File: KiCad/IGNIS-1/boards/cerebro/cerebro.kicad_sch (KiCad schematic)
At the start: 14 parts, among them J40 Backplane_2x10, J50 J_PWR_2x4, Q1 MMBT3904, U10 ESP32-WROOM-32E DevKit 40p

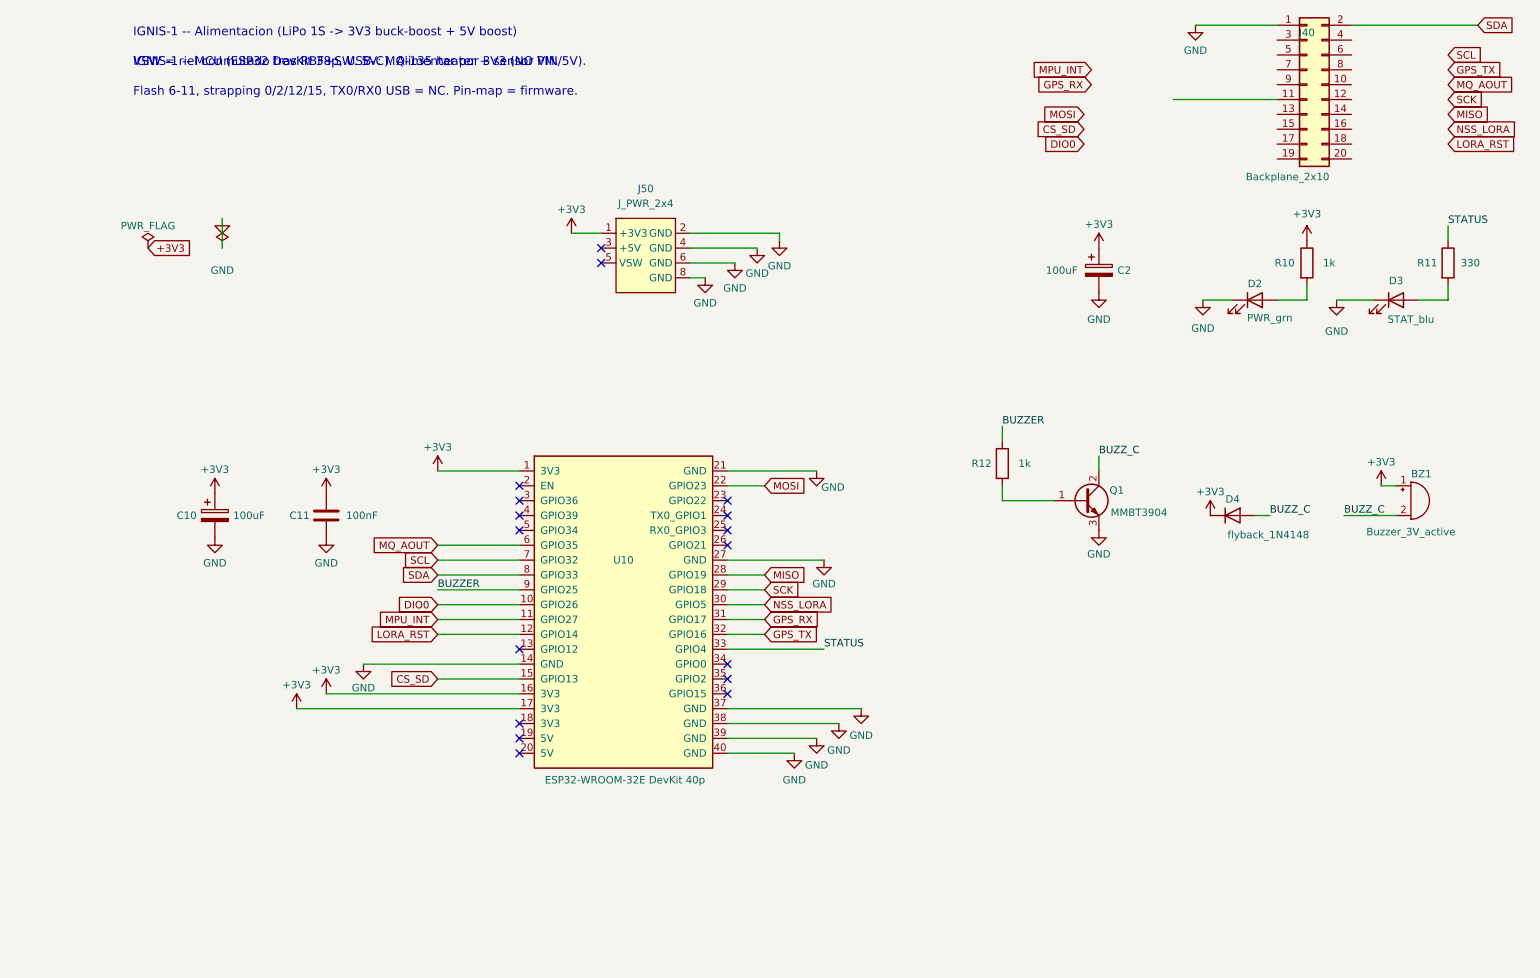
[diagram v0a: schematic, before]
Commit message: wip: recableo backplane split en progreso (GUI) + doc con move TPS63020
Co-Authored-By: Claude Opus 4.8 <noreply@anthropic.com>
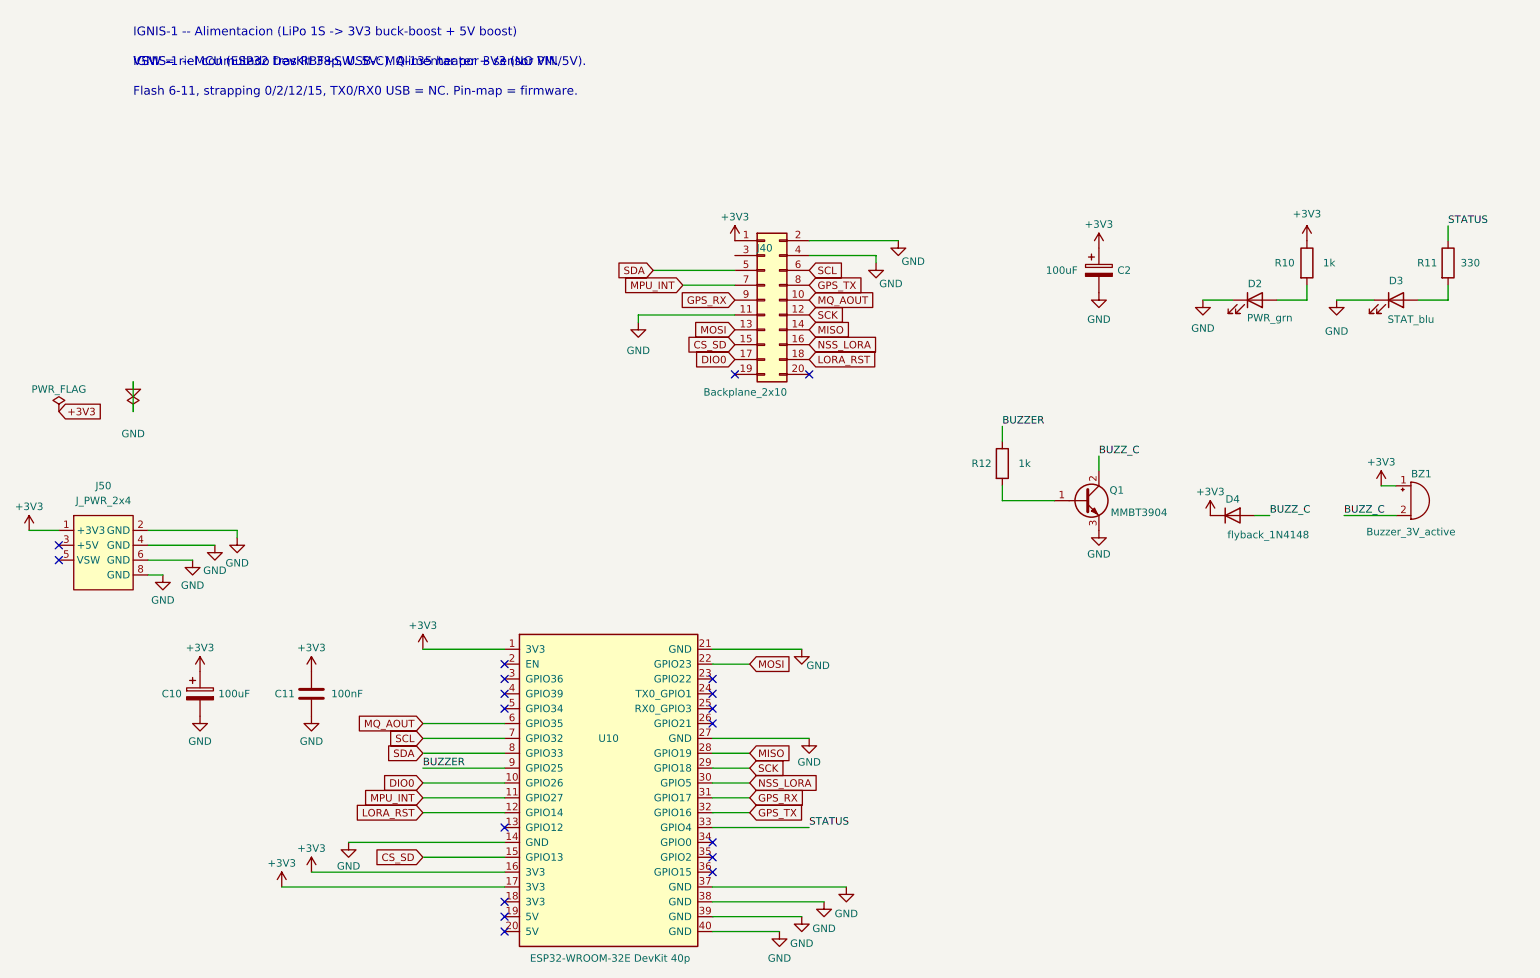
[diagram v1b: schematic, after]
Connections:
- net +3V3: now also J40.1 (Pin_1)
- net CS_SD: now also J40.15 (Pin_15)
- net DIO0: now also J40.17 (Pin_17)
- net GND: now also J40.11 (Pin_11), J40.2 (Pin_2), J40.4 (Pin_4); no longer J40.1 (Pin_1)
- net GPS_RX: now also J40.9 (Pin_9)
- net GPS_TX: now also J40.8 (Pin_8)
- net LORA_RST: now also J40.18 (Pin_18)
- net MISO: now also J40.14 (Pin_14)
- net MOSI: now also J40.13 (Pin_13)
- net MPU_INT: now also J40.7 (Pin_7)
- net MQ_AOUT: now also J40.10 (Pin_10)
- net NSS_LORA: now also J40.16 (Pin_16)
- net SCK: now also J40.12 (Pin_12)
- net SCL: now also J40.6 (Pin_6)
- net SDA: now also J40.5 (Pin_5); no longer J40.2 (Pin_2)
- no-connect marks 17 -> 19
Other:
- moved on the sheet: C10, C11, J40, J50, U10
